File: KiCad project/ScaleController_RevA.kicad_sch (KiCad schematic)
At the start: 26 parts, among them J1 USB_C_Receptacle, J2 JST_2mm_LiPo, U1 MCP73871, U2 LM1117MPX-3.3_NOPB

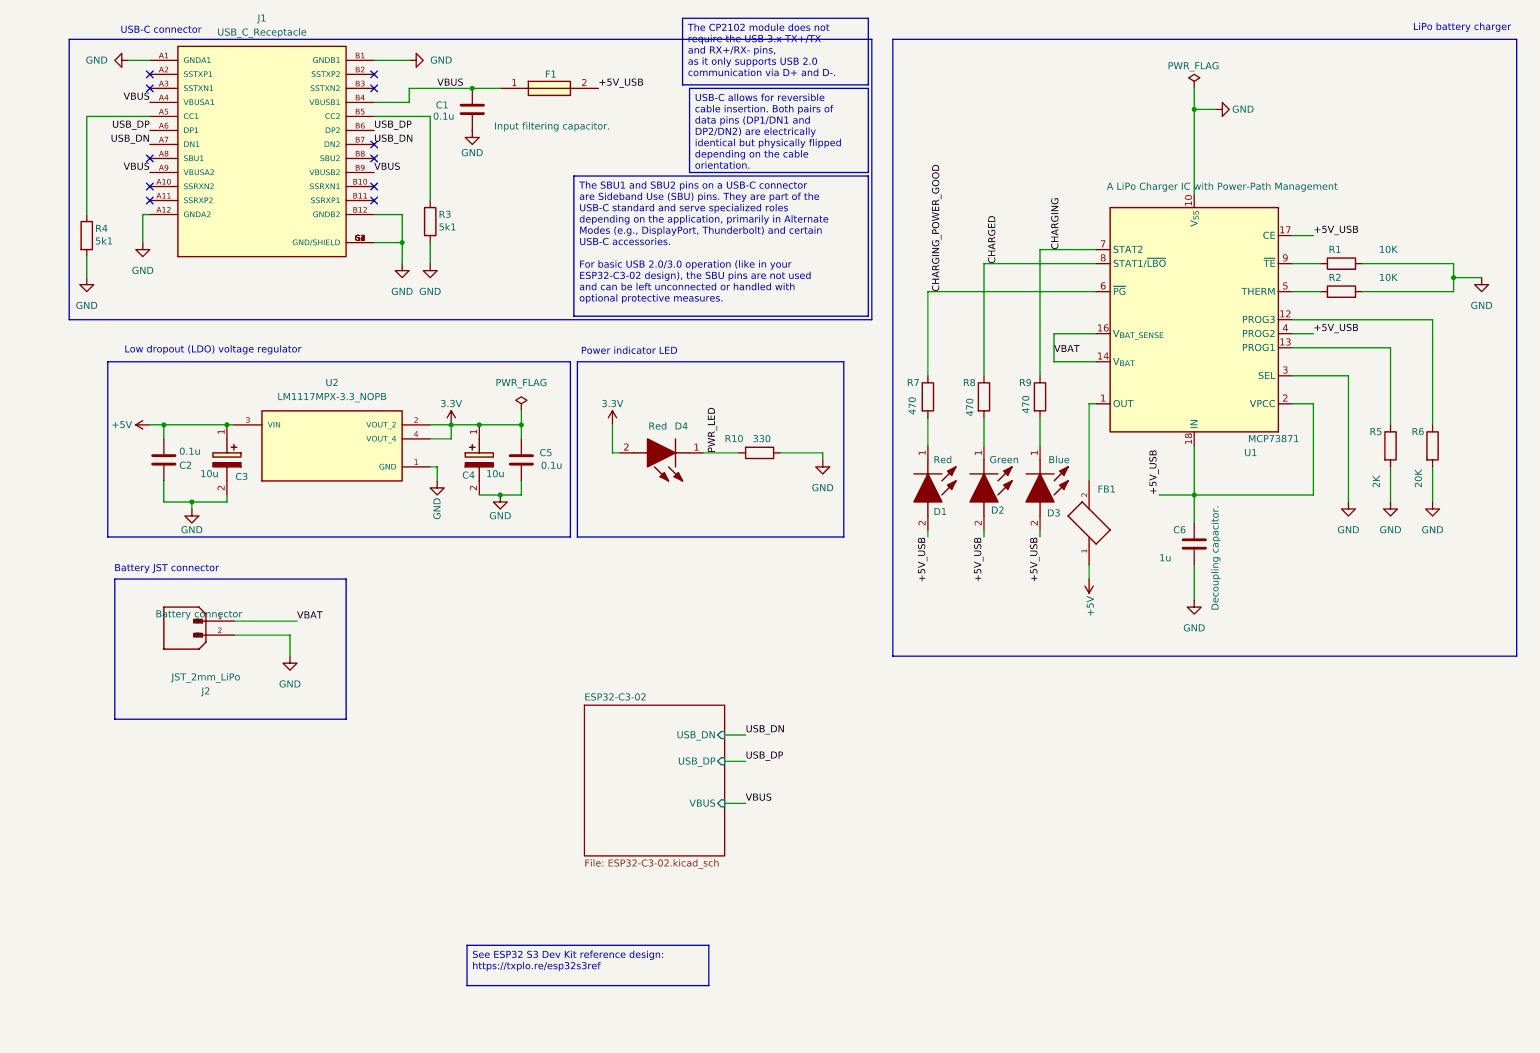
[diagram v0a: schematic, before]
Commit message: Add HX711 scale controller schematic and clean up legacy components
- Add HX711_LoadCell_Summing child sheet with 4x MTMM-103-03-T-S-150 load cell connectors, summing resistors, and decoupling caps
- Add OLED_Header child sheet (4-pin I2C socket for SSD1306)
- Remove battery charger (MCP73871), LiPo connector, mic preamp, BME280, SD card from schematic
- Reconnect power path: +5V_USB -> FB1 -> +5V -> LDO
- Add Samtec MTMM-103-03-T-S-150 footprint library to fp-lib-table
- Assign footprints to HX711 passives (C12-C17, R15/R16) and net ties (NT1-NT3)
- Update PCB from schematic: add new scale components, remove legacy footprints
- Track fp-lib-table in git (uses portable ${KIPRJMOD} paths)

Co-Authored-By: Claude Sonnet 4.6 <noreply@anthropic.com>
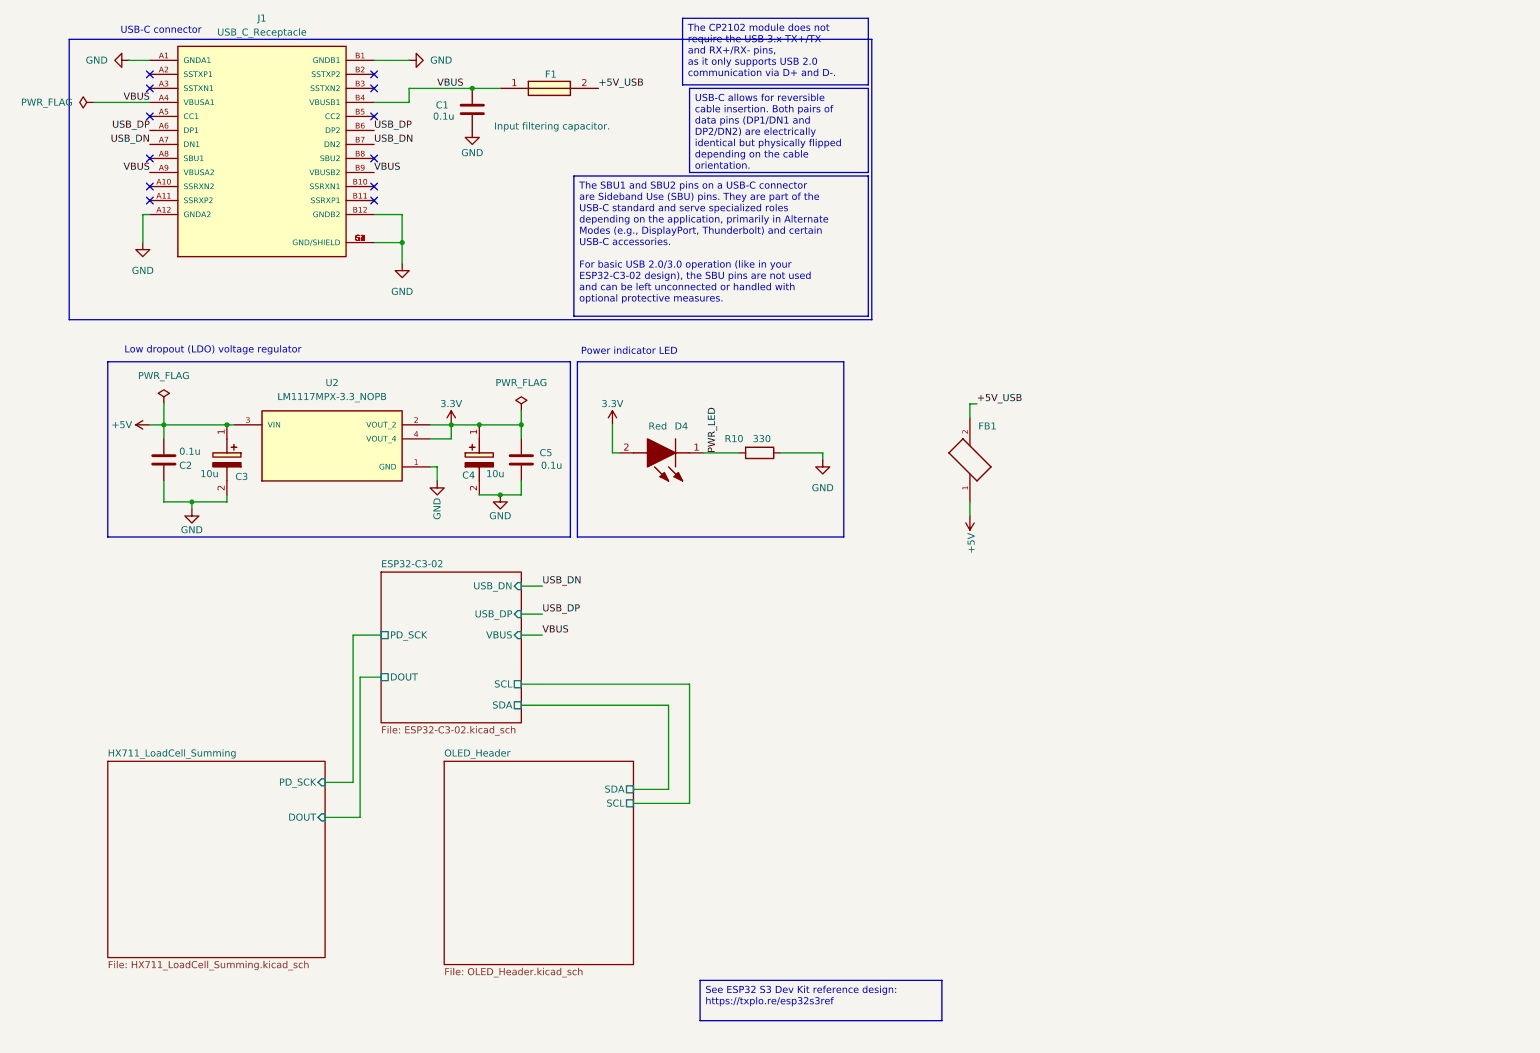
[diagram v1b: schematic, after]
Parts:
- removed C6: 1u, Capacitor_SMD:C_0805_2012Metric, symbol SparkFun-Capacitor:C
- removed D1: Red, Footprints:LEDC2012X120N, symbol LTST-C170KRKT:LTST-C170KRKT
- removed D2: Green, Footprints:LEDC2012X120N, symbol LTST-C170GKT:LTST-C170GKT
- removed D3: Blue, Footprints:LEDC2012X120N, symbol LTST-C170TBKT:LTST-C170TBKT
- removed J2: JST_2mm_LiPo, Footprints:JST_B2B-PH-SM4-TB, symbol B2B-PH-SM4-TB:B2B-PH-SM4-TB
- removed R1, R2: 10K, Resistor_SMD:R_0805_2012Metric, symbol Device:R
- removed R3, R4: 5k1, Resistor_SMD:R_0805_2012Metric, symbol Device:R
- removed R5: 2K, Resistor_SMD:R_0805_2012Metric, symbol Device:R
- removed R6: 20K, Resistor_SMD:R_0805_2012Metric, symbol Device:R
- removed R7, R8, R9: 470, Resistor_SMD:R_0805_2012Metric, symbol Device:R
- removed U1: MCP73871, Package_DFN_QFN:QFN-20-1EP_4x4mm_P0.5mm_EP2.5x2.5mm, symbol Battery_Management:MCP73871
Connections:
- net +5V_USB: now also FB1.2
- no-connect marks 11 -> 12
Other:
- added sheet HX711_LoadCell_Summing (HX711_LoadCell_Summing.kicad_sch)
- added sheet OLED_Header (OLED_Header.kicad_sch)
- sheet ESP32-C3-02 ports: added DOUT, PD_SCK, SCL, SDA; removed none
- note removed: "Battery JST connector"
- note removed: "LiPo battery charger"
- company: Tech Explorations -> (none)
- moved on the sheet: FB1

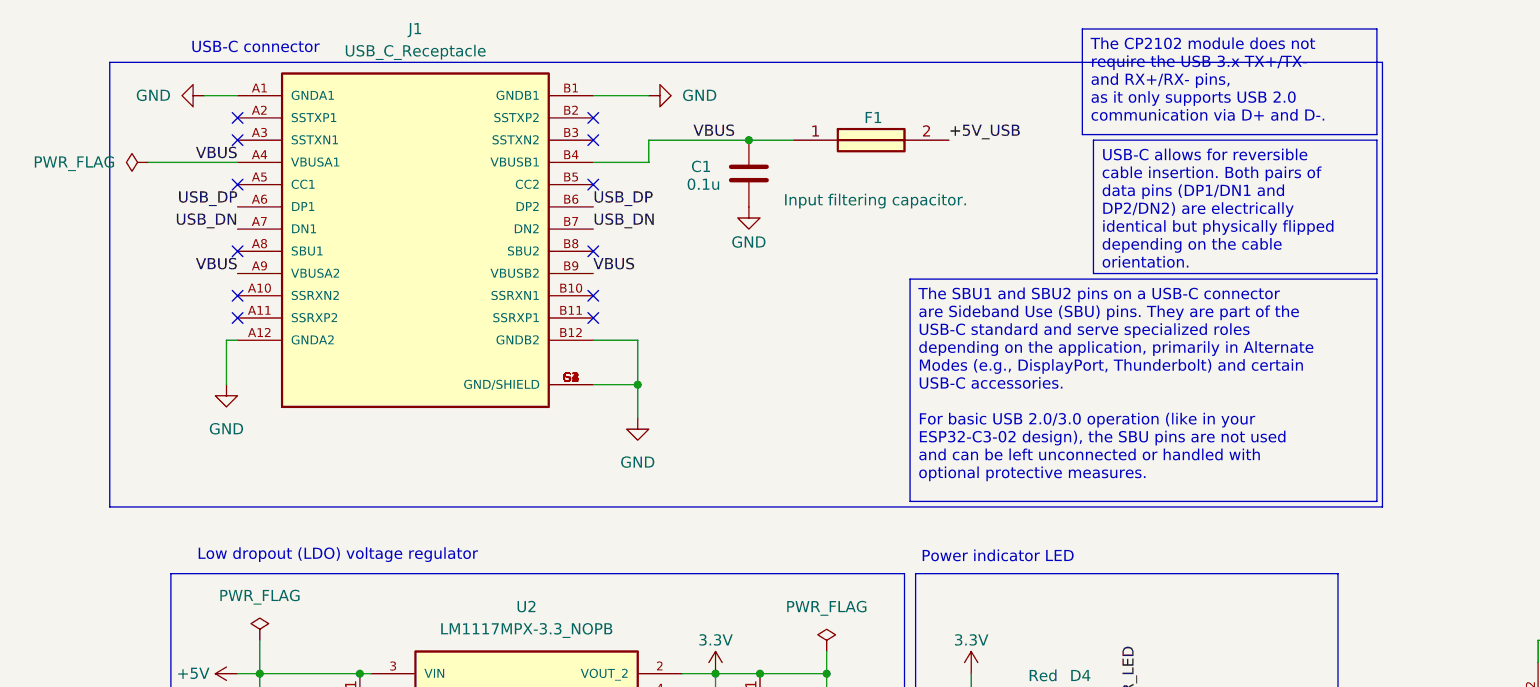
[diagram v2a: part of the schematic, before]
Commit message: USB-C: HRO TYPE-C-31-M-12 receptacle, CC pull-downs, VBUS/GND short removed
J1 replaced by Connector:USB_C_Receptacle_USB2.0_16P with the
Connector_USB HRO TYPE-C-31-M-12 footprint (SMD signal pins, 4 PTH
shell legs) in place of the Bel SS-52400-002, whose staggered PTH row
(0.35 mm hole spacing, 0.10 mm rings) fell below PCBWay's normal process.
Added R1/R2 5.1k CC1/CC2 pull-downs so the board powers from USB-C
chargers and C-to-C cables. Removed a leftover wire that bridged C1 and
shorted VBUS to GND after the edit. 57 nets, ERC 0 errors.

Co-Authored-By: Claude Fable 5.1 <noreply@anthropic.com>
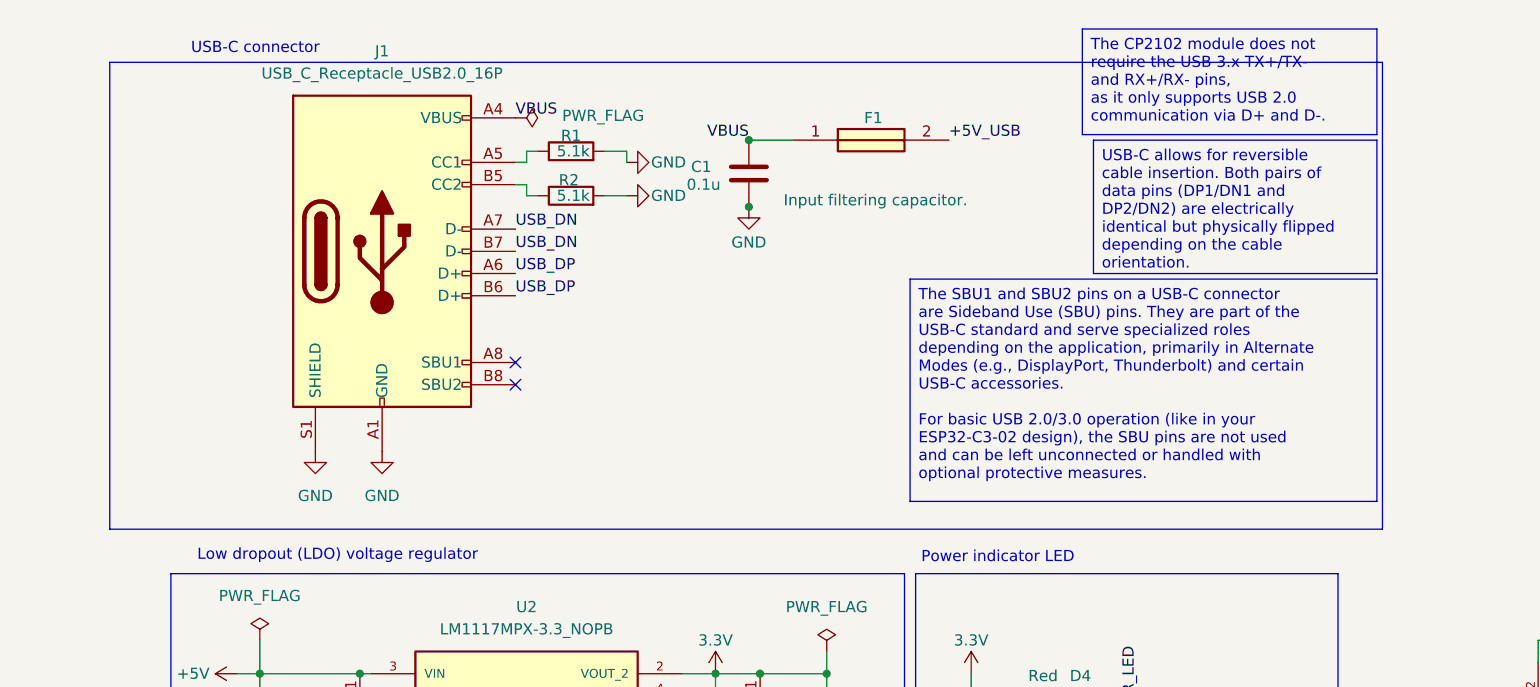
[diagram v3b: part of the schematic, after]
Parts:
- removed J1: USB_C_Receptacle, Footprints:BELFUSE_SS-52400-002, symbol SS-52400-002:SS-52400-002
- added J1: USB_C_Receptacle_USB2.0_16P, Connector_USB:USB_C_Receptacle_HRO_TYPE-C-31-M-12, symbol Connector:USB_C_Receptacle_USB2.0_16P
- added R1, R2: 5.1k, Resistor_SMD:R_0805_2012Metric, symbol Device:R
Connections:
- net GND: now also J1.A1 (GND), J1.A12 (GND), J1.B1 (GND), J1.B12 (GND), J1.S1 (SHIELD), R1.2, R2.2
- net USB_DN: now also J1.A7 (D-), J1.B7 (D-)
- net USB_DP: now also J1.A6 (D+), J1.B6 (D+)
- net VBUS: now also J1.A4 (VBUS), J1.A9 (VBUS), J1.B4 (VBUS), J1.B9 (VBUS)
- new net: J1.A5 (CC1), R1.1
- new net: J1.B5 (CC2), R2.1
- no-connect marks 12 -> 2

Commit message: OLED header J9 on the back side with the module's pin order
J9 rewired to 1=GND 2=3V3 3=SCL 4=SDA (the order on the 0.96in Hosyond
I2C module) and flipped to the bottom side, so the module plugs in from
below and lies flat under the board, clear of the load-cell sockets.
SCL/SDA tails re-routed to the swapped pads; 3V3/GND land on the planes.
J9 labels reordered on top and duplicated mirrored on the back. The
DISP1 placeholder now models the 0.96in module (27 x 27.5 mm) under the
board, replacing the 1.3in upright placeholder.

Fills stale in this commit (refill in GUI). Enclosure note: standoffs
under the board need >= 14 mm for the module.

Co-Authored-By: Claude Fable 5.1 <noreply@anthropic.com>
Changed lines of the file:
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@@
-	)
-	(junction
-		(at 87.63 34.29)
-		(diameter 0)
-		(color 0 0 0 0)
 	)
 	(junction
@@
 		(diameter 0)
 		(color 0 0 0 0)
-	)
-	(junction
-		(at 87.63 26.67)
-		(diameter 0)
-		(color 0 0 0 0)

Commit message: Pre-order tidy: DRU, symbol-lib sync, PCBWay stackup, JST part number on J3/5/7/8
- .kicad_dru: drop the global annular_width ignore. U3's ground-grid pads
  are 0.6/0.3 mm since the DFM pass; DRC is identical without the rule.
- Project symbol libs for LM1117MPX-3.3_NOPB, ESP32-C3-WROOM-02-H4 and
  MTMM-103-03-T-S-150 rewritten in KiCad 9 format from the schematic
  copies (the MTMM copy has pins 1/2/3 to match the JST PH pads; the old
  lib still had 01/02/03). SnapEDA "Description_1" junk fields removed
  from libs, embedded copies and instances. ERC: 0 lib_symbol_mismatch.
- Stackup: PCBWay standard 4-layer 1.6 mm (7628 prepreg 0.19 x2,
  core 1.03, 1 oz all layers).
- J3/J5/J7/J8: Value/MF/MP -> JST B3B-PH-K-S in schematic, project lib
  and board footprints; stale Samtec/SnapEDA fields dropped. Symbol name
  and lib_id left as MTMM-103-03-T-S-150.

Netlist nets/pins identical before and after. DRC with schematic parity:
0 errors, 0 unconnected, 0 parity issues, 5 known benign warnings.

Co-Authored-By: Claude Fable 5.1 <noreply@anthropic.com>
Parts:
- U2: Description_1 800-mA 15-V linear voltage regulator -> (none)
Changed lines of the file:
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@@
-			)
-		)
-		(property "Description_1" "\n                        \n                            800-mA 15-V linear voltage regulator\n                        \n"
-			(at 62.23 90.17 0)
-			(effects
-				(font
-					(size 1.27 1.27)
-				)
-				(justify bottom)
-				(hide yes)
 			)
 		)

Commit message: BOM fixes, DRC exclusions, edge-clearance restore, fab outputs and order notes
- C9 value 4.7u -> 10u (matches its KEMET T491A 10 uF part number; LM1117
  output cap). Capacitor values normalised to 0.1u / 1u / 10u so identical
  0805 parts group: BOM 30 -> 27 lines.
- J1 value -> HRO TYPE-C-31-M-12, MF/MP fields added (schematic + board).
- min_copper_edge_clearance restored to 0.3 mm. The DFM commit 4617449 set
  it; the GUI refill save in 61ca090 wrote the old project file back (0.2).
  Board meets 0.3 (probe rule: no violations).
- DRC exclusions for the 4 silk-over-edge warnings (J1 face, U3 antenna
  notch), added in the GUI.
- docs/pcbway-order-notes.md: board spec, stackup, drills, special notes.
- docs/status-2026-09-18.md: supersedes 17 Sept; kicad-cli regen commands.
- TODO: fabrication items ticked.

Fab package generated to fabrication/RevA-2026-09-18/ (git-ignored):
schematic PDF, BOM (raw + PCBWay), Gerbers/drill zip, pos top/bottom.
Netlist nets/pins identical to bdae270. DRC + parity: 0 errors,
0 unconnected, 0 parity; 4 excluded + 1 intentional warning.

Co-Authored-By: Claude Fable 5.1 <noreply@anthropic.com>
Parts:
- J1: value USB_C_Receptacle_USB2.0_16P -> TYPE-C-31-M-12; MF (none) -> HRO; MP (none) -> TYPE-C-31-M-12
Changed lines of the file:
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@@
 			)
 		)
-		(property "Value" "USB_C_Receptacle_USB2.0_16P"
+		(property "Value" "TYPE-C-31-M-12"
 			(at 45.72 19.05 0)
 			(effects
@@
 			(at 49.53 39.37 0)
 			(effects
+				(font
+					(size 1.27 1.27)
+				)
+				(hide yes)
+			)
+		)
+		(property "MF" "HRO"
+			(at 49.53 39.37 0)
+			(effects
+				(font
+					(size 1.27 1.27)
+				)
+				(hide yes)
+			)
+		)
+		(property "MP" "TYPE-C-31-M-12"
+			(at 49.53 39.37 0)
+			(effects
